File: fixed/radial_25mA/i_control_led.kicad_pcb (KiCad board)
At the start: 2 copper layers, 25.4 x 20 mm, 18 parts, among them J1 Conn_01x04, J2 Conn_01x04, M1 MountingHole_2.5mm_Pad, M2 MountingHole_2.5mm_Pad, M3 MountingHole_2.5mm_Pad, M4 MountingHole_2.5mm_Pad, Q1 MMBT5551L, U1 LM2775DSG, U2 LMV321

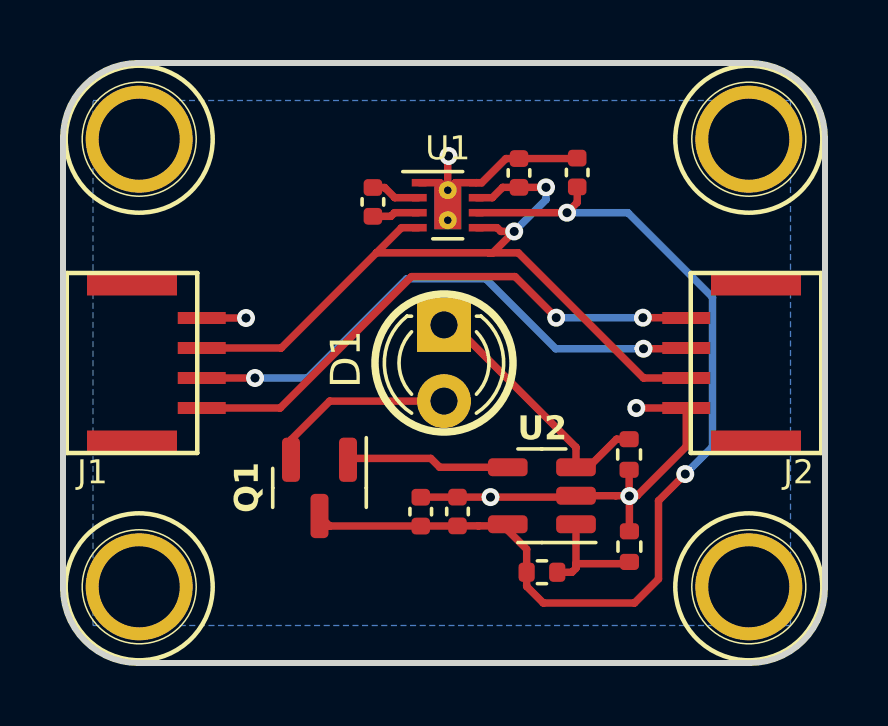
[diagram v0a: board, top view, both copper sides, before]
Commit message: Work on rev2 of fixed 25mA radial design.
Finished layout, routing and fab files.
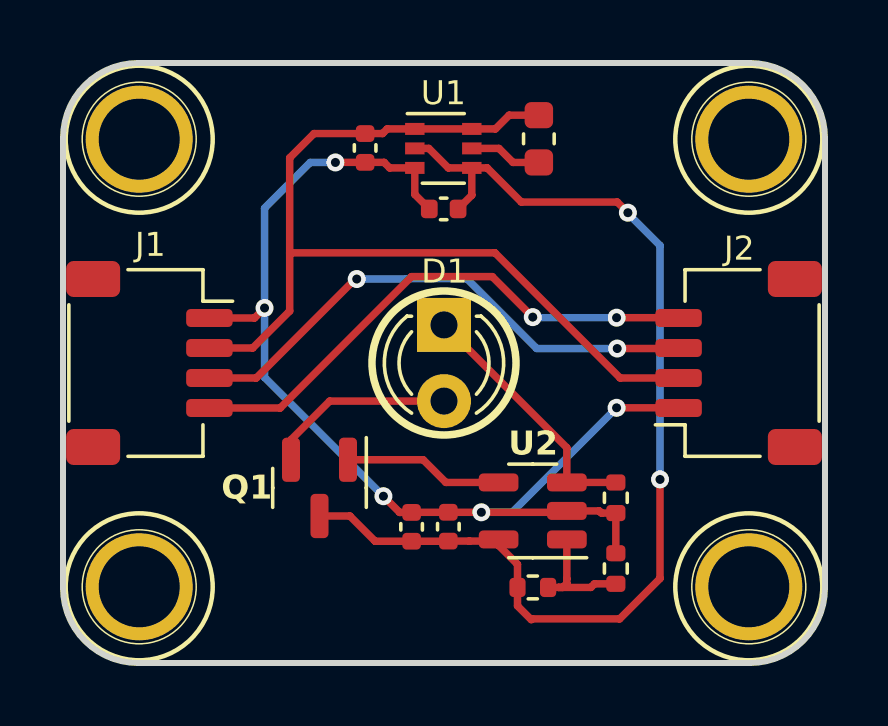
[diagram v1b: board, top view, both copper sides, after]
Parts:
- removed the C3 at (67.1, 53.6)
- added L1: 4.7uF, Inductor_SMD:L_0603_1608Metric, F.Cu at (65.9, 52.5)
- C2: value 1uF -> 10uF
- D1: value LED_ALT -> LED; footprint LED_THT:LED_D3.0mm -> LED_D3mm_custom:LED_D3.0mm
- J1, J2: footprint BOOMELE_SH_SMD:BOOMELE_SMD_SH_4PIN_RT -> JST_SH_SM04B_custom:JST_SH_SM04B-SRSS-TB_1x04-1MP_P1.00mm_Horizontal
- R1: value 100 -> 10
- R2: value 10k -> 20k
- R3: value 10k -> 1k
- U1: value LM2775DSG -> TPS61222DCK; footprint Package_SON:WSON-8-1EP_2x2mm_P0.5mm_EP0.9x1.6mm_ThermalVias -> Package_TO_SOT_SMD:SOT-363_SC-70-6
- moved C1 5.20 mm to (60.1, 52.8), turned to 90 degrees
- moved C2 2.37 mm to (62.7, 54.9), turned to 0 degrees
- moved U1 1.90 mm to (62.7, 52.8)
- moved R1 1.51 mm to (68.4, 64.5)
- moved R3 0.86 mm to (68.4, 66.9)
- moved C3 0.59 mm to (62.8, 65.5)
- moved C4 0.59 mm to (61.6, 65.5)
- moved R2 0.59 mm to (65.7, 67.5)
- moved U2 0.59 mm to (65.7, 64.9)
- moved J2 0.10 mm to (72.5, 60.0), turned to 90 degrees
- moved J1 0.10 mm to (52.9, 60.0), turned to -90 degrees
- renumbered C4 to C3, C5 to C4
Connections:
- C2 pad 1: Net-(U1-C1+) -> GND
- C2 pad 2: Net-(U1-C1-) -> /5V
- U1 pad 1: GND -> /VIN
- U1 pad 2: Net-(U1-C1-) -> /5V
- U1 pad 3: Net-(U1-C1+) -> GND
- U1 pad 4: /VIN -> /5V
- U1 pad 5: /VIN -> /VL
- U1 pad 6: /5V -> /VIN
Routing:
- net GND: track 22.8 -> 37.8 mm
- net /VIN: track 27.8 -> 31.7 mm, vias 2 -> 0
- net /5V: track 33.9 -> 37.0 mm
- net /VL: track 0.00 -> 2.43 mm
- net Net-(U1-C1-): track 1.69 -> 0.00 mm
- net Net-(U1-C1+): track 1.59 -> 0.00 mm
- net /SCL: track 18.5 -> 17.9 mm
- net /SDA: track 18.5 -> 17.9 mm
- removed copper zone on B.Cu, net GND
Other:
- board text added: "IControl LED V0.1 R2 www.iorodeo.com Radial, I=24mA Vin=3.3-5.0V"
- board text removed: "IControl LED V0.1 R1 www.iorodeo.com Radial, I=25mA Vin=3.3-5V"
